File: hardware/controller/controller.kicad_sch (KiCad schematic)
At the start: 0 parts

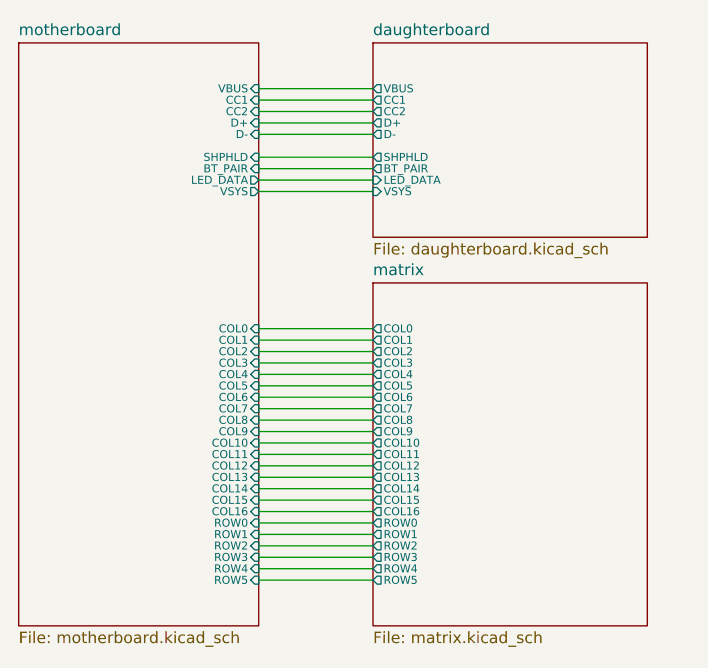
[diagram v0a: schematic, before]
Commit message: refactor(controller): remove matrix sheet (moved to membrane)
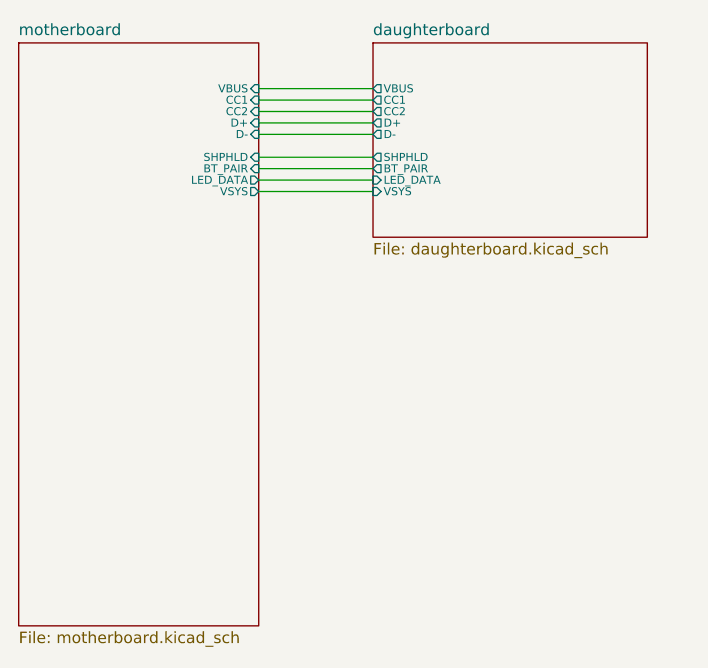
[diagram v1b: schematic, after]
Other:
- removed sheet matrix
- sheet motherboard ports: added none; removed COL0, COL1, COL10, COL11, COL12, COL13, COL14, COL15, COL16, COL2, COL3, COL4, COL5, COL6, COL7, COL8, COL9, ROW0, ROW1, ROW2, ROW3, ROW4, ROW5
